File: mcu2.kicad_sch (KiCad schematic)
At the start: 90 parts, among them J100 Conn_01x01, J101 Conn_01x01, J102 Conn_01x01, J103 Conn_01x01, J104 Conn_01x01, J105 Conn_01x01, J108 Conn_01x01, J109 Conn_01x01, J110 Conn_01x01, J1106 Conn_01x01, J1107 Conn_01x01, J111 Conn_01x01, J112 Conn_01x01, J113 Conn_01x01, J114 Conn_01x01, J115 Conn_01x01, J116 Conn_01x01, J117 Conn_01x01, J118 Conn_01x01, J119 Conn_01x01, J120 Conn_01x01, J121 Conn_01x01, J122 Conn_01x01, J123 Conn_01x22, J78 Conn_01x22, J79 Conn_01x01, J80 Conn_01x01, J81 Conn_01x01, J82 Conn_01x01, J83 Conn_01x01, J84 Conn_01x01, J85 Conn_01x01, J86 Conn_01x01, J87 Conn_01x01, J88 Conn_01x01, J89 Conn_01x01, J90 Conn_01x01, J91 Conn_01x01, J92 Conn_01x01, J93 Conn_01x01, J94 Conn_01x01, J95 Conn_01x01, J96 Conn_01x01, J97 Conn_01x01, J98 Conn_01x01, J99 Conn_01x01

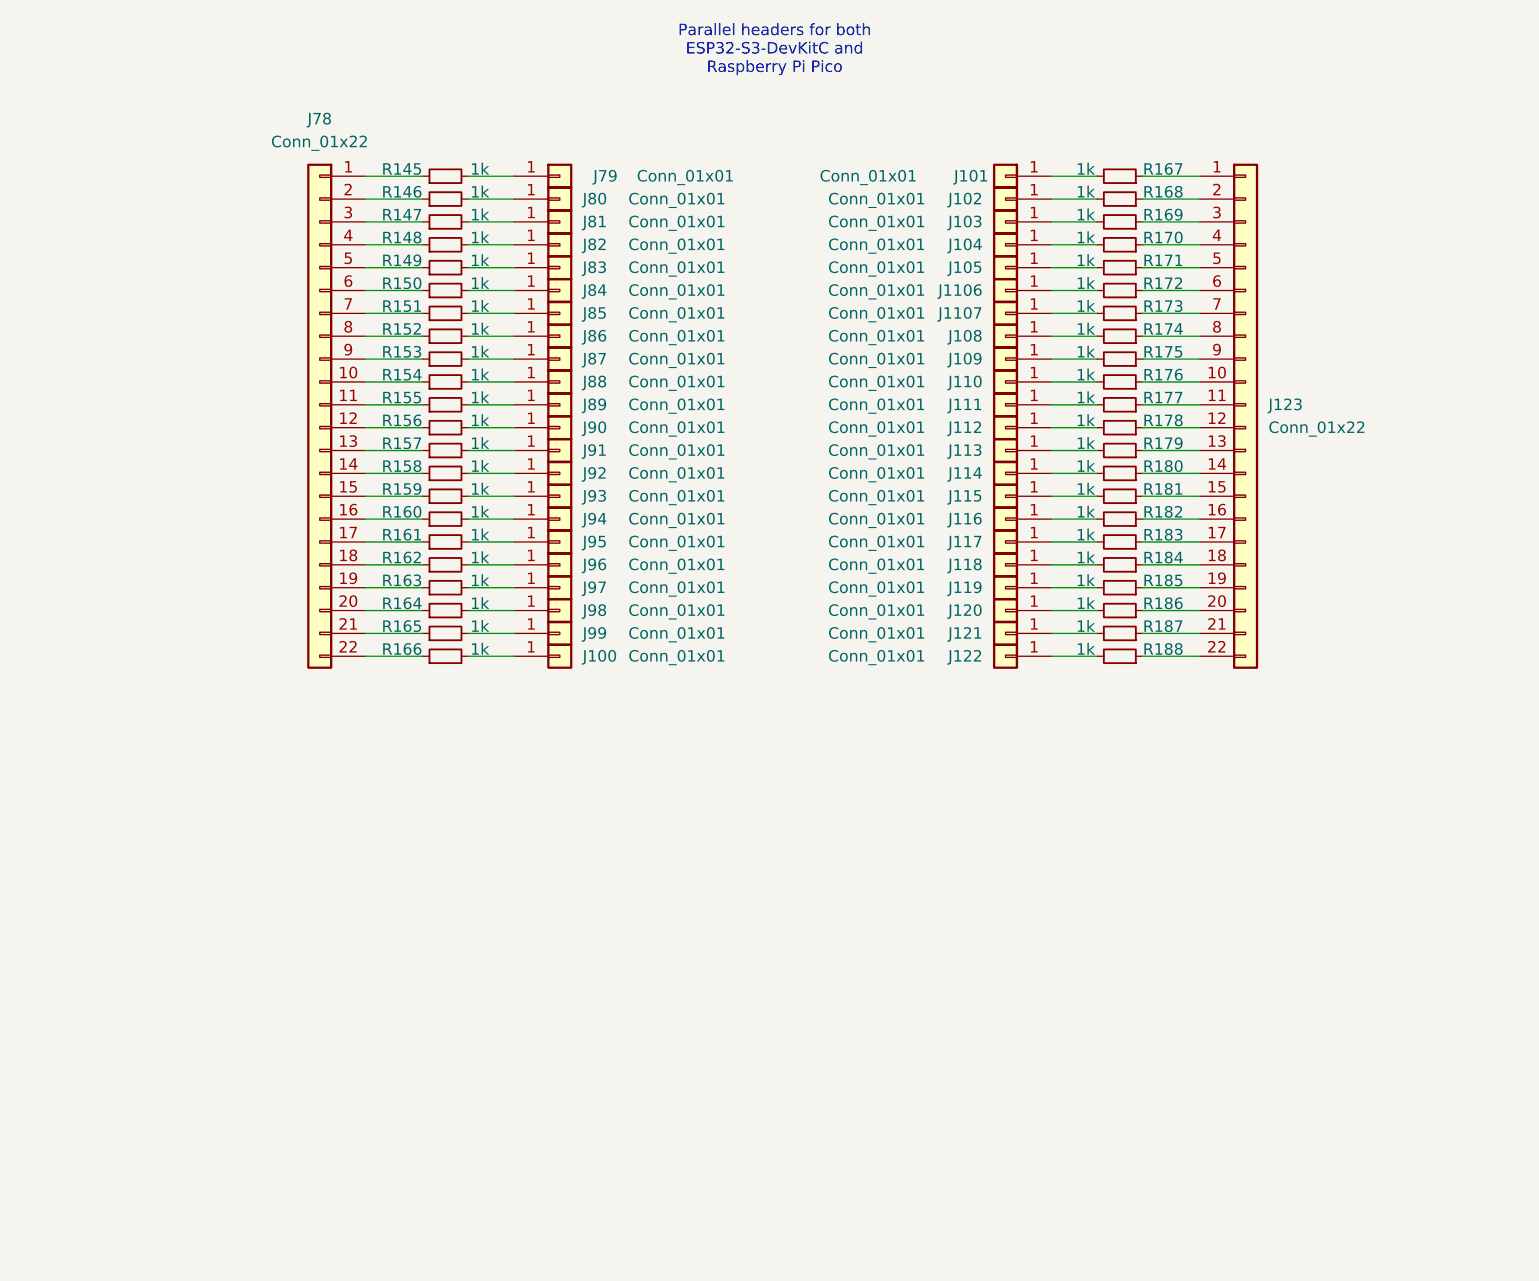
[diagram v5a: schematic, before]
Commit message: Update the design to a stackable one
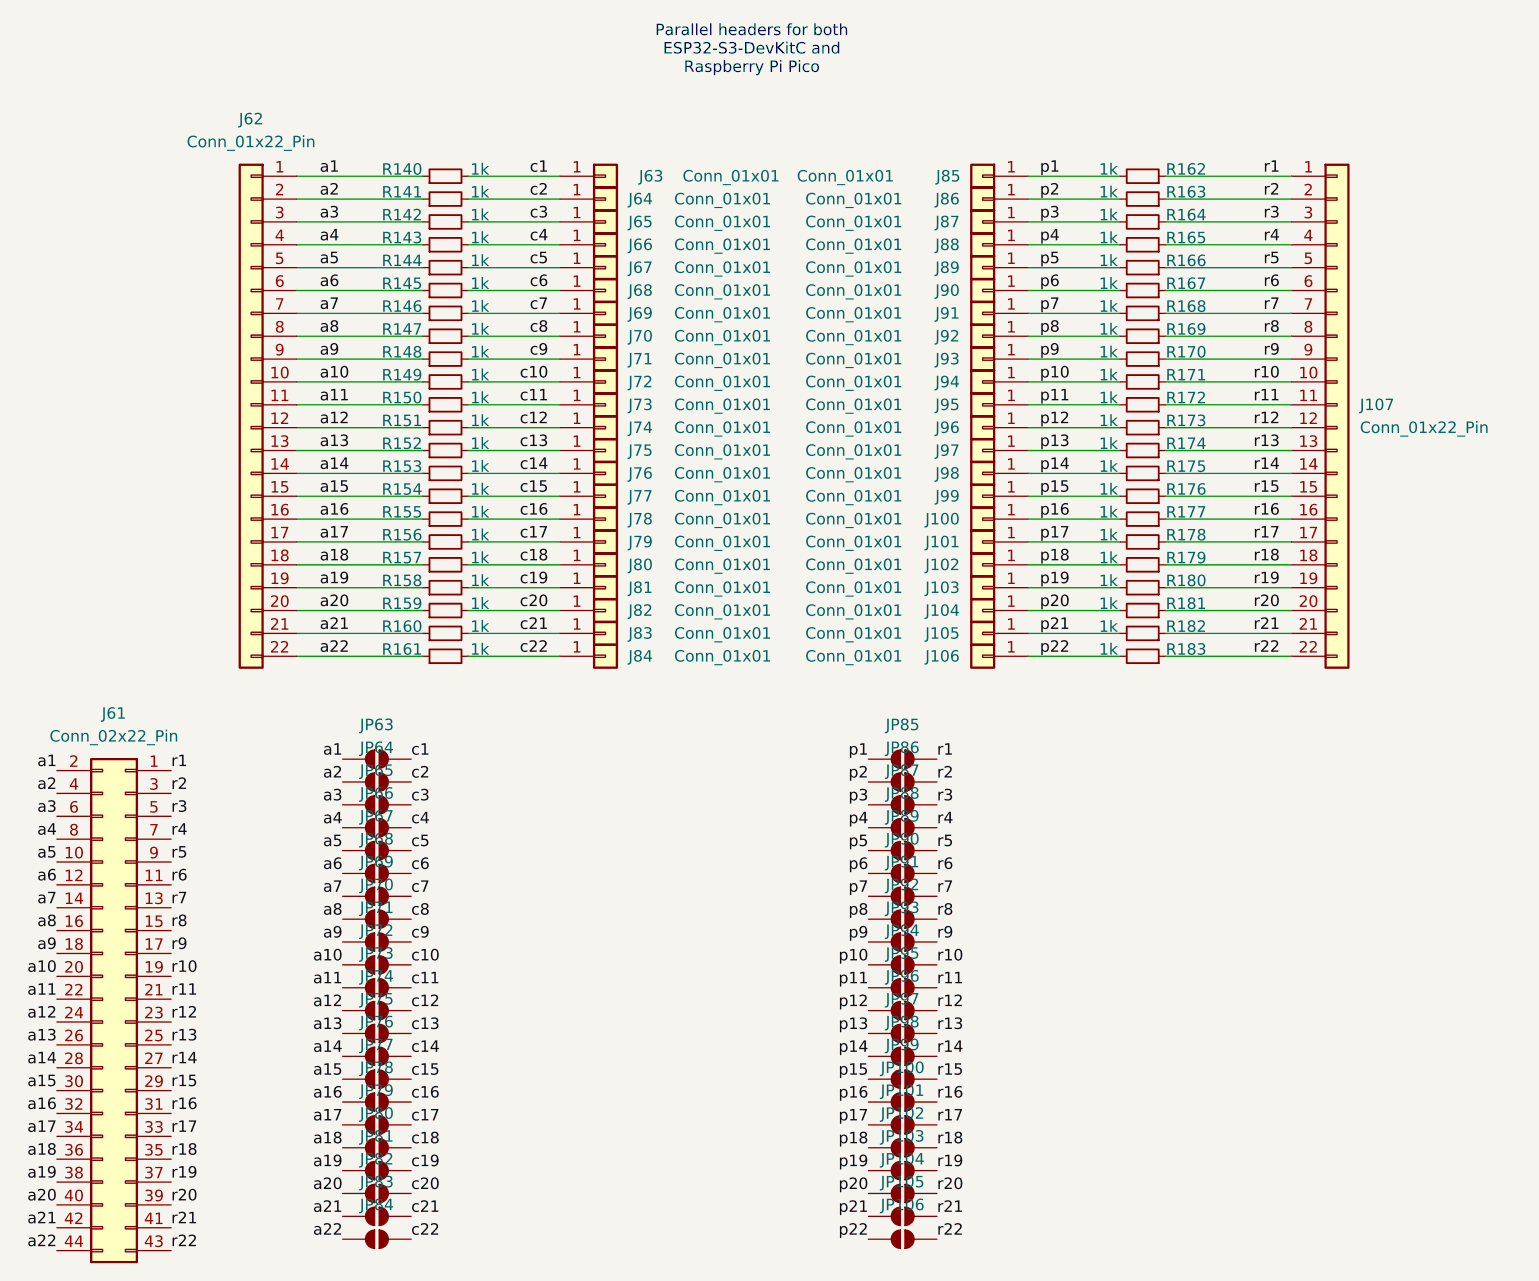
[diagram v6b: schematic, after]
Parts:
- added J61: Conn_02x22_Pin, HL_Connector_Pad_2.54mm:Pad_2x22_P2.54_1.7x1.7_Oct, symbol Connector_Generic:Conn_02x22_Odd_Even
- added JP100, JP101, JP102, JP103, JP104, JP105, JP106, JP63, JP64, JP65, JP66, JP67, JP68, JP69, JP70, JP71, JP72, JP73, JP74, JP75, JP76, JP77, JP78, JP79, JP80, JP81, JP82, JP83, JP84, JP85, JP86, JP87, JP88, JP89, JP90, JP91, JP92, JP93, JP94, JP95, JP96, JP97, JP98, JP99: SolderJumper_2_Open, Jumper:SolderJumper-2_P1.3mm_Open_TrianglePad1.0x1.5mm, symbol Jumper:SolderJumper_2_Open
- J107: renamed from J123; value Conn_01x22 -> Conn_01x22_Pin; JLCPCB_CORRECTION (none) -> 0;-29.21;270; LCSC (none) -> C7430378
- J62: renamed from J78; value Conn_01x22 -> Conn_01x22_Pin; JLCPCB_CORRECTION (none) -> 0;-29.21;270; LCSC (none) -> C7430378
- renumbered J116 to J100, J117 to J101, J118 to J102, J119 to J103, J120 to J104, J121 to J105, J122 to J106, J79 to J63, J80 to J64, J81 to J65, J82 to J66, J83 to J67, J84 to J68, J85 to J69, J86 to J70, J87 to J71, J88 to J72, J89 to J73, J90 to J74, J91 to J75, J92 to J76, J93 to J77, J94 to J78, J95 to J79, J96 to J80, J97 to J81, J98 to J82, J99 to J83, J100 to J84, J101 to J85, J102 to J86, J103 to J87, J104 to J88, J105 to J89, J1106 to J90, J1107 to J91, J108 to J92, J109 to J93, J110 to J94, J111 to J95, J112 to J96, J113 to J97, J114 to J98, J115 to J99, R145 to R140, R146 to R141, R147 to R142, R148 to R143, R149 to R144, R150 to R145, R151 to R146, R152 to R147, R153 to R148, R154 to R149, R155 to R150, R156 to R151, R157 to R152, R158 to R153, R159 to R154, R160 to R155, R161 to R156, R162 to R157, R163 to R158, R164 to R159, R165 to R160, R166 to R161, R167 to R162, R168 to R163, R169 to R164, R170 to R165, R171 to R166, R172 to R167, R173 to R168, R174 to R169, R175 to R170, R176 to R171, R177 to R172, R178 to R173, R179 to R174, R180 to R175, R181 to R176, R182 to R177, R183 to R178, R184 to R179, R185 to R180, R186 to R181, R187 to R182, R188 to R183
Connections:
- net a11: now reaches J62.11 (Pin_11), R150.1
- net a11: now also J61.22 (Pin_22), JP73.1 (A)
- net c11: now reaches J73.1 (Pin_1), R150.2
- net c11: now also JP73.2 (B)
- net c5: now reaches J67.1 (Pin_1), R144.2
- net c5: now also JP67.2 (B)
- net c12: now reaches J74.1 (Pin_1), R151.2
- net c12: now also JP74.2 (B)
- net p15: now reaches J99.1 (Pin_1), R176.2
- net p15: now also JP99.1 (A)
- net r9: now reaches J107.9 (Pin_9), R170.1
- net r9: now also J61.17 (Pin_17), JP93.2 (B)
- net p9: now reaches J93.1 (Pin_1), R170.2
- net p9: now also JP93.1 (A)
- net r1: now reaches J107.1 (Pin_1), R162.1
- net r1: now also J61.1 (Pin_1), JP85.2 (B)
- net r10: now reaches J107.10 (Pin_10), R171.1
- net r10: now also J61.19 (Pin_19), JP94.2 (B)
- net r11: now reaches J107.11 (Pin_11), R172.1
- net r11: now also J61.21 (Pin_21), JP95.2 (B)
- net r12: now reaches J107.12 (Pin_12), R173.1
- net r12: now also J61.23 (Pin_23), JP96.2 (B)
- net r13: now reaches J107.13 (Pin_13), R174.1
- net r13: now also J61.25 (Pin_25), JP97.2 (B)
- net r14: now reaches J107.14 (Pin_14), R175.1
- net r14: now also J61.27 (Pin_27), JP98.2 (B)
- net r15: now reaches J107.15 (Pin_15), R176.1
- net r15: now also J61.29 (Pin_29), JP99.2 (B)
- net r16: now reaches J107.16 (Pin_16), R177.1
- net r16: now also J61.31 (Pin_31), JP100.2 (B)
- net r17: now reaches J107.17 (Pin_17), R178.1
- net r17: now also J61.33 (Pin_33), JP101.2 (B)
- net r18: now reaches J107.18 (Pin_18), R179.1
- net r18: now also J61.35 (Pin_35), JP102.2 (B)
- net r19: now reaches J107.19 (Pin_19), R180.1
- net r19: now also J61.37 (Pin_37), JP103.2 (B)
- net r2: now reaches J107.2 (Pin_2), R163.1
- net r2: now also J61.3 (Pin_3), JP86.2 (B)
- net r20: now reaches J107.20 (Pin_20), R181.1
- net r20: now also J61.39 (Pin_39), JP104.2 (B)
- net r21: now reaches J107.21 (Pin_21), R182.1
- net r21: now also J61.41 (Pin_41), JP105.2 (B)
- net r22: now reaches J107.22 (Pin_22), R183.1
- net r22: now also J61.43 (Pin_43), JP106.2 (B)
- net r3: now reaches J107.3 (Pin_3), R164.1
- net r3: now also J61.5 (Pin_5), JP87.2 (B)
- net r4: now reaches J107.4 (Pin_4), R165.1
- net r4: now also J61.7 (Pin_7), JP88.2 (B)
- net r5: now reaches J107.5 (Pin_5), R166.1
- net r5: now also J61.9 (Pin_9), JP89.2 (B)
- net r6: now reaches J107.6 (Pin_6), R167.1
- net r6: now also J61.11 (Pin_11), JP90.2 (B)
- net r7: now reaches J107.7 (Pin_7), R168.1
- net r7: now also J61.13 (Pin_13), JP91.2 (B)
- net r8: now reaches J107.8 (Pin_8), R169.1
- net r8: now also J61.15 (Pin_15), JP92.2 (B)
- net a22: now reaches J62.22 (Pin_22), R161.1
- net a22: now also J61.44 (Pin_44), JP84.1 (A)
- net c22: now reaches J84.1 (Pin_1), R161.2
- net c22: now also JP84.2 (B)
- net c9: now reaches J71.1 (Pin_1), R148.2
- net c9: now also JP71.2 (B)
- net p20: now reaches J104.1 (Pin_1), R181.2
- net p20: now also JP104.1 (A)
- net p5: now reaches J89.1 (Pin_1), R166.2
- net p5: now also JP89.1 (A)
- net c4: now reaches J66.1 (Pin_1), R143.2
- net c4: now also JP66.2 (B)
- net c1: now reaches J63.1 (Pin_1), R140.2
- net c1: now also JP63.2 (B)
- net a21: now reaches J62.21 (Pin_21), R160.1
- net a21: now also J61.42 (Pin_42), JP83.1 (A)
- net c21: now reaches J83.1 (Pin_1), R160.2
- net c21: now also JP83.2 (B)
- net p16: now reaches J100.1 (Pin_1), R177.2
- net p16: now also JP100.1 (A)
- net p8: now reaches J92.1 (Pin_1), R169.2
- net p8: now also JP92.1 (A)
- net a18: now reaches J62.18 (Pin_18), R157.1
- net a18: now also J61.36 (Pin_36), JP80.1 (A)
- net c18: now reaches J80.1 (Pin_1), R157.2
- net c18: now also JP80.2 (B)
- net p22: now reaches J106.1 (Pin_1), R183.2
- net p22: now also JP106.1 (A)
- net c10: now reaches J72.1 (Pin_1), R149.2
- net c10: now also JP72.2 (B)
- net p12: now reaches J96.1 (Pin_1), R173.2
- net p12: now also JP96.1 (A)
- net p18: now reaches J102.1 (Pin_1), R179.2
- net p18: now also JP102.1 (A)
- net c19: now reaches J81.1 (Pin_1), R158.2
- net c19: now also JP81.2 (B)
- net p2: now reaches J86.1 (Pin_1), R163.2
- net p2: now also JP86.1 (A)
- net p1: now reaches J85.1 (Pin_1), R162.2
- net p1: now also JP85.1 (A)
- net p10: now reaches J94.1 (Pin_1), R171.2
- net p10: now also JP94.1 (A)
- net p21: now reaches J105.1 (Pin_1), R182.2
- net p21: now also JP105.1 (A)
- net c3: now reaches J65.1 (Pin_1), R142.2
- net c3: now also JP65.2 (B)
- net p3: now reaches J87.1 (Pin_1), R164.2
- net p3: now also JP87.1 (A)
- net a5: now reaches J62.5 (Pin_5), R144.1
- net a5: now also J61.10 (Pin_10), JP67.1 (A)
- net p13: now reaches J97.1 (Pin_1), R174.2
- net p13: now also JP97.1 (A)
- net a15: now reaches J62.15 (Pin_15), R154.1
- net a15: now also J61.30 (Pin_30), JP77.1 (A)
- net c15: now reaches J77.1 (Pin_1), R154.2
- net c15: now also JP77.2 (B)
- net c8: now reaches J70.1 (Pin_1), R147.2
- net c8: now also JP70.2 (B)
- net a19: now reaches J62.19 (Pin_19), R158.1
- net a19: now also J61.38 (Pin_38), JP81.1 (A)
- net a1: now reaches J62.1 (Pin_1), R140.1
- net a1: now also J61.2 (Pin_2), JP63.1 (A)
- net a20: now reaches J62.20 (Pin_20), R159.1
- net a20: now also J61.40 (Pin_40), JP82.1 (A)
- net c20: now reaches J82.1 (Pin_1), R159.2
- net c20: now also JP82.2 (B)
- net p19: now reaches J103.1 (Pin_1), R180.2
- net p19: now also JP103.1 (A)
- net p17: now reaches J101.1 (Pin_1), R178.2
- net p17: now also JP101.1 (A)
- net a13: now reaches J62.13 (Pin_13), R152.1
- net a13: now also J61.26 (Pin_26), JP75.1 (A)
- net c13: now reaches J75.1 (Pin_1), R152.2
- net c13: now also JP75.2 (B)
- net a10: now reaches J62.10 (Pin_10), R149.1
- net a10: now also J61.20 (Pin_20), JP72.1 (A)
- net a12: now reaches J62.12 (Pin_12), R151.1
- net a12: now also J61.24 (Pin_24), JP74.1 (A)
- net a14: now reaches J62.14 (Pin_14), R153.1
- net a14: now also J61.28 (Pin_28), JP76.1 (A)
- net a16: now reaches J62.16 (Pin_16), R155.1
- net a16: now also J61.32 (Pin_32), JP78.1 (A)
- net a17: now reaches J62.17 (Pin_17), R156.1
- net a17: now also J61.34 (Pin_34), JP79.1 (A)
- net a2: now reaches J62.2 (Pin_2), R141.1
- net a2: now also J61.4 (Pin_4), JP64.1 (A)
- net a3: now reaches J62.3 (Pin_3), R142.1
- net a3: now also J61.6 (Pin_6), JP65.1 (A)
- net a4: now reaches J62.4 (Pin_4), R143.1
- net a4: now also J61.8 (Pin_8), JP66.1 (A)
- net a6: now reaches J62.6 (Pin_6), R145.1
- net a6: now also J61.12 (Pin_12), JP68.1 (A)
- net a7: now reaches J62.7 (Pin_7), R146.1
- net a7: now also J61.14 (Pin_14), JP69.1 (A)
- net a8: now reaches J62.8 (Pin_8), R147.1
- net a8: now also J61.16 (Pin_16), JP70.1 (A)
- net a9: now reaches J62.9 (Pin_9), R148.1
- net a9: now also J61.18 (Pin_18), JP71.1 (A)
- net p14: now reaches J98.1 (Pin_1), R175.2
- net p14: now also JP98.1 (A)
- net p6: now reaches J90.1 (Pin_1), R167.2
- net p6: now also JP90.1 (A)
- net p11: now reaches J95.1 (Pin_1), R172.2
- net p11: now also JP95.1 (A)
- net c6: now reaches J68.1 (Pin_1), R145.2
- net c6: now also JP68.2 (B)
- net c17: now reaches J79.1 (Pin_1), R156.2
- net c17: now also JP79.2 (B)
- net c7: now reaches J69.1 (Pin_1), R146.2
- net c7: now also JP69.2 (B)
- net c14: now reaches J76.1 (Pin_1), R153.2
- net c14: now also JP76.2 (B)
- net c16: now reaches J78.1 (Pin_1), R155.2
- net c16: now also JP78.2 (B)
- net c2: now reaches J64.1 (Pin_1), R141.2
- net c2: now also JP64.2 (B)
- net p7: now reaches J91.1 (Pin_1), R168.2
- net p7: now also JP91.1 (A)
- net p4: now reaches J88.1 (Pin_1), R165.2
- net p4: now also JP88.1 (A)
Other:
- moved on the sheet: J100, J101, J102, J103, J104, J105, J106, J107, J62, J63, J64, J65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
